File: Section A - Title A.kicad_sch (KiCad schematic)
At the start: 0 parts

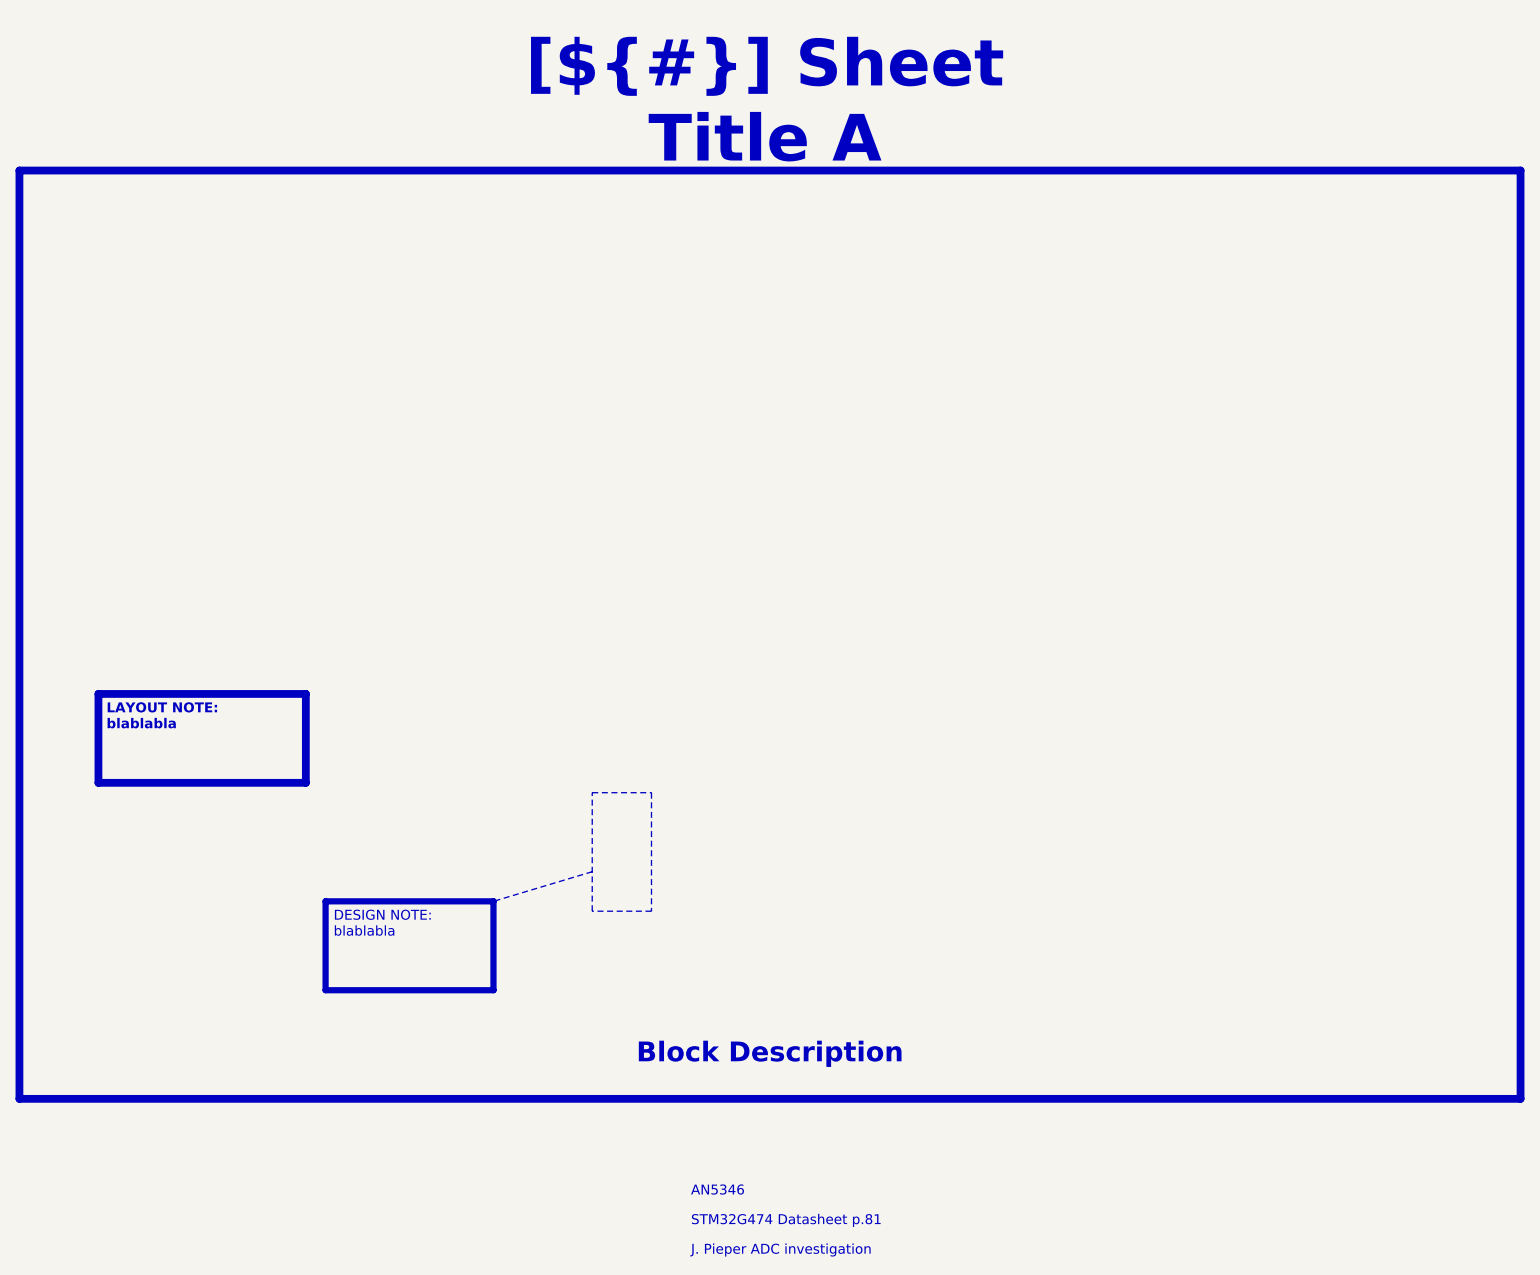
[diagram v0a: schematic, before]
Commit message: [added] completed initial sch design, move from draft to preliminary
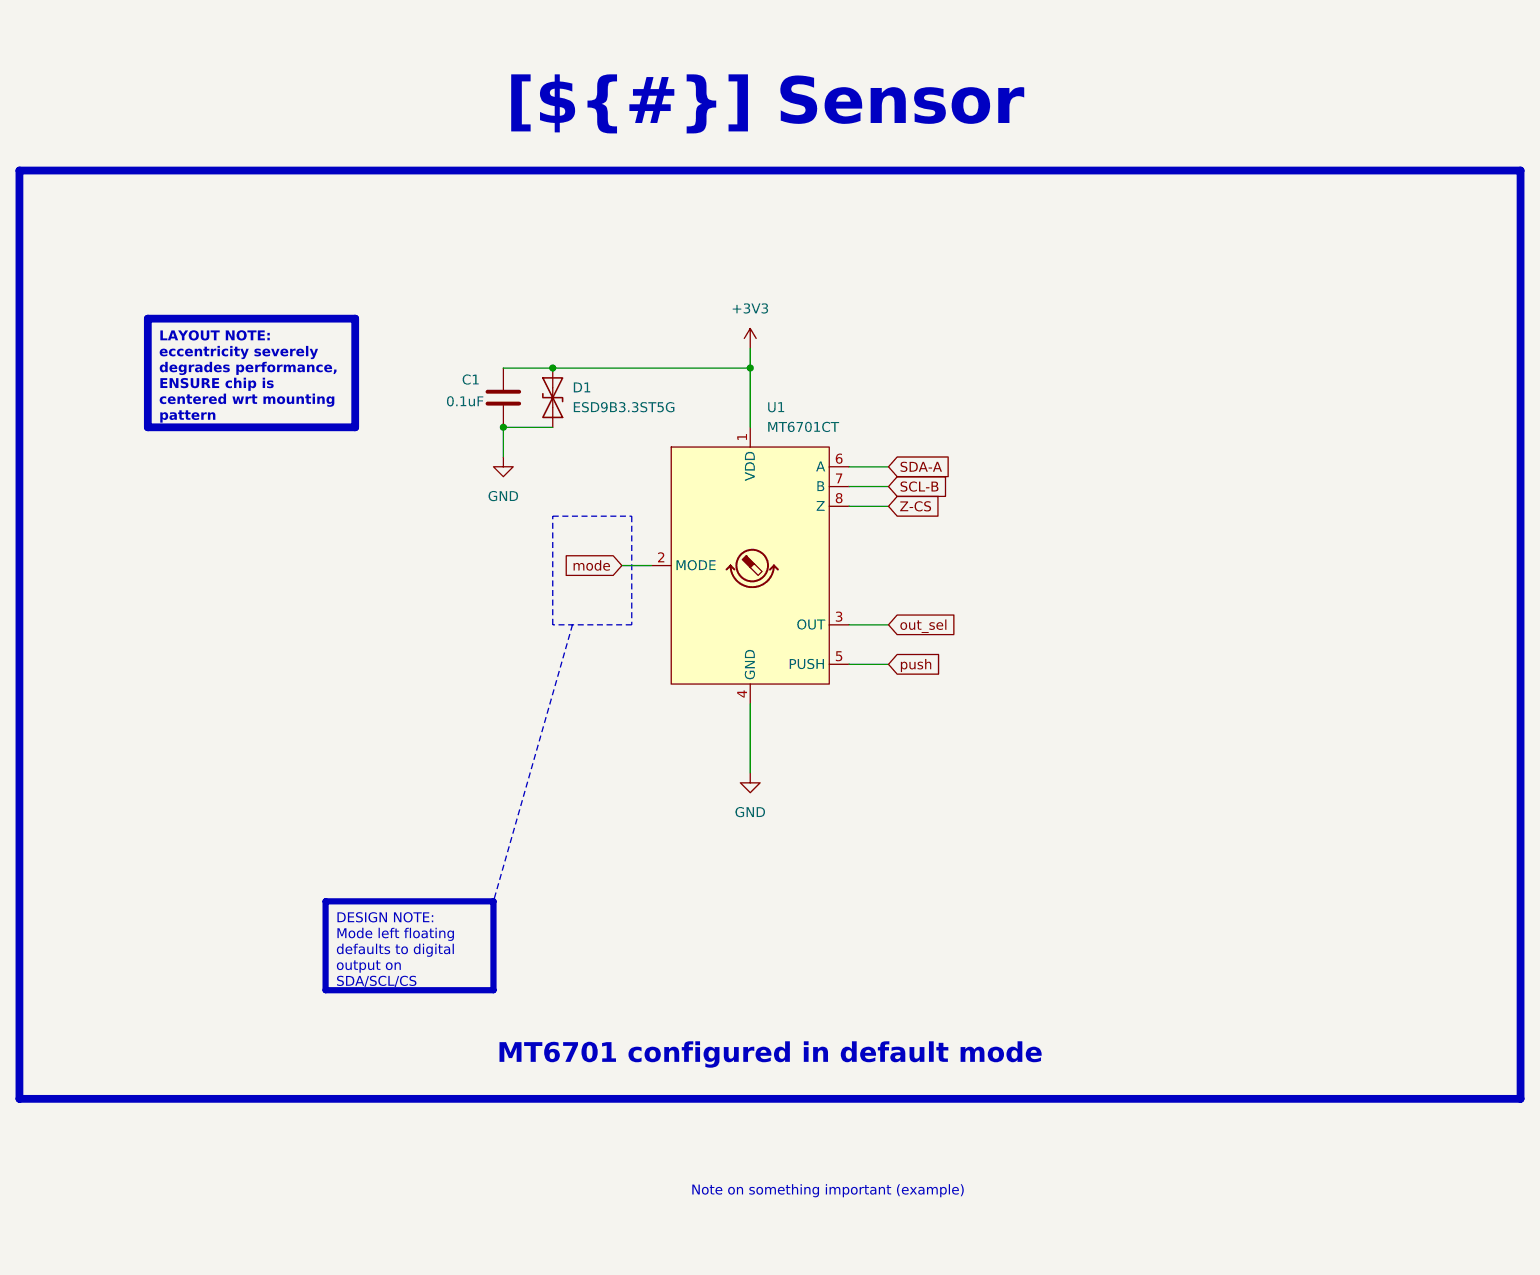
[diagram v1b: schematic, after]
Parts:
- added C1: 0.1uF, Capacitor_SMD:C_0603_1608Metric, symbol Device:C
- added D1: ESD9B3.3ST5G, Diode_SMD:D_SOD-923, symbol Diode:ESD9B3.3ST5G
- added U1: MT6701CT, Package_SO:SO-8_3.9x4.9mm_P1.27mm, symbol Sensor_Magnetic:MT6701CT
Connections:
- new net +3V3: C1.1, D1.2 (A2), U1.1 (VDD)
- new net GND: C1.2, D1.1 (A1), U1.4 (GND)
- new net SCL-B: U1.7 (B)
- new net SDA-A: U1.6 (A)
- new net Z-CS: U1.8 (Z)
- new net mode: U1.2 (MODE)
- new net out_sel: U1.3 (OUT)
- new net push: U1.5 (PUSH)
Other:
- note added: "Note on something important (example)"
- note removed: "AN5346"
- note removed: "J. Pieper ADC investigation"
- note removed: "STM32G474 Datasheet p.81"
- title: Sheet Title A -> Sensor
